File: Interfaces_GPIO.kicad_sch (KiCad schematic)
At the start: 5 parts, among them U3 MCP23008-xP

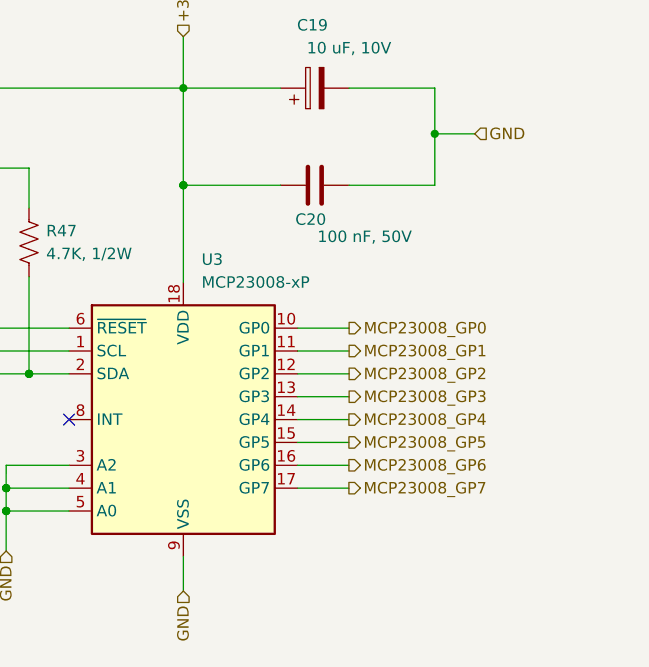
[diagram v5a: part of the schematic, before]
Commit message: Se finalizó con el PCB del prototipo.
Dado que se buscó a toda costa que el PCB fuera de 1 capa, en varios puntos del circuito se tuvieron que agregar pin headers individuales para conectar a 3V3 y GND, junto con tiras de pin headers. Cada una de estas se conectara luego entre si mediante cables.

Tambien se generaron los archivos Gerber y BOM.
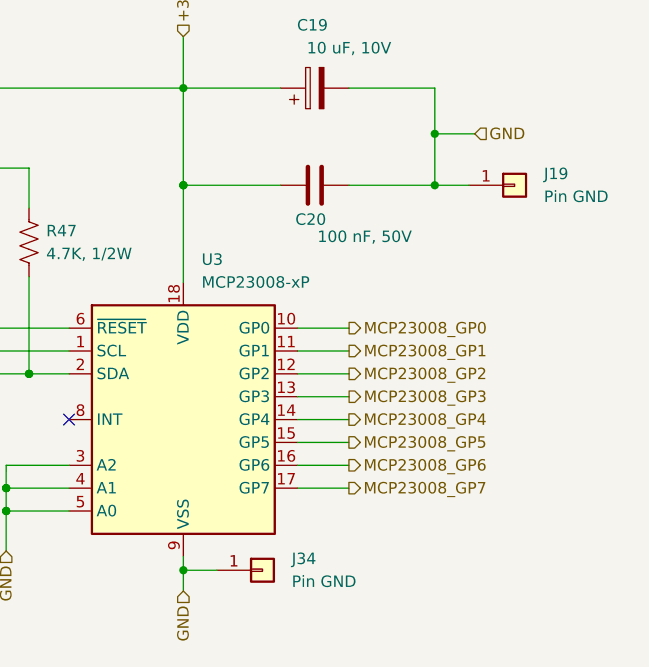
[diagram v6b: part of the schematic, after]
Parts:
- added J19, J34: Pin GND, Connector_PinHeader_2.54mm:PinHeader_1x01_P2.54mm_Vertical, symbol Connector_Generic:Conn_01x01
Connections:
- net GND: now also J19.1 (Pin_1), J34.1 (Pin_1)
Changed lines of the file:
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@@
 (kicad_sch (version 20211123) (generator eeschema)
   (paper "A4")
+  (junction (at 147.9804 131.0386) (diameter 0) (color 0 0 0 0)
+  )
   (junction (at 128.2954 124.46) (diameter 0) (color 0 0 0 0)
   )
@@
   )
   (junction (at 128.2903 124.46) (diameter 0) (color 0 0 0 0)
+  )
+  (junction (at 175.9153 88.265) (diameter 0) (color 0 0 0 0)
   )
   (junction (at 119.4003 106.68) (diameter 0) (color 0 0 0 0)
@@
     (stroke (width 0) (type default) (color 0 0 0 0))
   )
-  (wire (pts (xy 175.9153 88.265) (xy 166.3903 88.265))
+  (wire (pts (xy 166.3903 88.265) (xy 175.9153 88.265))
     (stroke (width 0) (type default) (color 0 0 0 0))
   )
@@
     (stroke (width 0) (type default) (color 0 0 0 0))
   )
+  (wire (pts (xy 175.9153 88.265) (xy 179.705 88.265))
+    (stroke (width 0) (type default) (color 0 0 0 0))
+  )
   (wire (pts (xy 128.2954 121.92) (xy 128.2903 121.92))
     (stroke (width 0) (type default) (color 0 0 0 0))
@@
     (stroke (width 0) (type default) (color 0 0 0 0))
   )
+  (wire (pts (xy 147.9804 131.0386) (xy 147.9804 133.35))
+    (stroke (width 0) (type default) (color 0 0 0 0))
+  )
   (wire (pts (xy 112.4153 106.68) (xy 119.4003 106.68))
     (stroke (width 0) (type default) (color 0 0 0 0))
@@
     (stroke (width 0) (type default) (color 0 0 0 0))
   )
-  (wire (pts (xy 147.9804 129.54) (xy 147.9804 133.35))
+  (wire (pts (xy 147.9804 129.54) (xy 147.9804 131.0386))
     (stroke (width 0) (type default) (color 0 0 0 0))
   )
@@
   )
   (wire (pts (xy 130.8303 86.36) (xy 130.8303 90.805))
+    (stroke (width 0) (type default) (color 0 0 0 0))
+  )
+  (wire (pts (xy 147.9804 131.0386) (xy 151.6888 131.0386))
     (stroke (width 0) (type default) (color 0 0 0 0))
   )
@@
   (hierarchical_label "+3,3V" (shape input) (at 147.9753 71.755 90)
     (effects (font (size 1.27 1.27)) (justify left))
+  )
+  (symbol (lib_id "Connector_Generic:Conn_01x01") (at 184.785 88.265 0) (unit 1)
+    (in_bom yes) (on_board yes) (fields_autoplaced)
+    (property "Reference" "J19" (id 0) (at 188.0362 86.9949 0)
+      (effects (font (size 1.27 1.27)) (justify left))
+    )
+    (property "Value" "Pin GND" (id 1) (at 188.0362 89.5349 0)
+      (effects (font (size 1.27 1.27)) (justify left))
+    )
+    (property "Footprint" "Connector_PinHeader_2.54mm:PinHeader_1x01_P2.54mm_Vertical" (id 2) (at 184.785 88.265 0)
+      (effects (font (size 1.27 1.27)) hide)
+    )
+    (property "Datasheet" "~" (id 3) (at 184.785 88.265 0)
+      (effects (font (size 1.27 1.27)) hide)
+    )
+    (pin "1")
   )
   (symbol (lib_id "Device:C") (at 162.5803 88.265 90) (unit 1)
@@
     (pin "9")
   )
+  (symbol (lib_id "Connector_Generic:Conn_01x01") (at 156.7688 131.0386 0) (unit 1)
+    (in_bom yes) (on_board yes) (fields_autoplaced)
+    (property "Reference" "J34" (id 0) (at 160.02 129.7685 0)
+      (effects (font (size 1.27 1.27)) (justify left))
+    )
+    (property "Value" "Pin GND" (id 1) (at 160.02 132.3085 0)
+      (effects (font (size 1.27 1.27)) (justify left))
+    )
+    (property "Footprint" "Connector_PinHeader_2.54mm:PinHeader_1x01_P2.54mm_Vertical" (id 2) (at 156.7688 131.0386 0)
+      (effects (font (size 1.27 1.27)) hide)
+    )
+    (property "Datasheet" "~" (id 3) (at 156.7688 131.0386 0)
+      (effects (font (size 1.27 1.27)) hide)
+    )
+    (pin "1")
+  )
 )

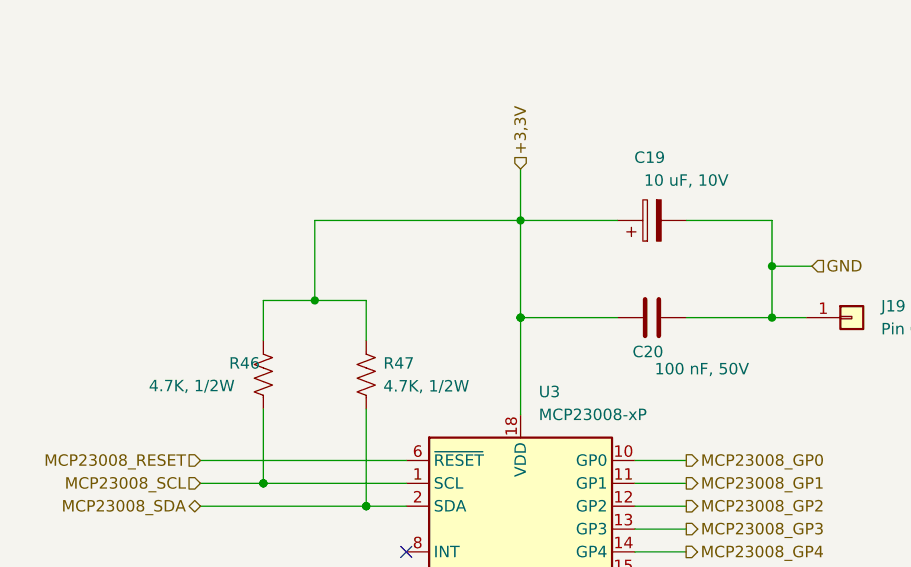
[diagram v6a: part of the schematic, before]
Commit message: Se modificaron algunos componentes, según disponibilidad
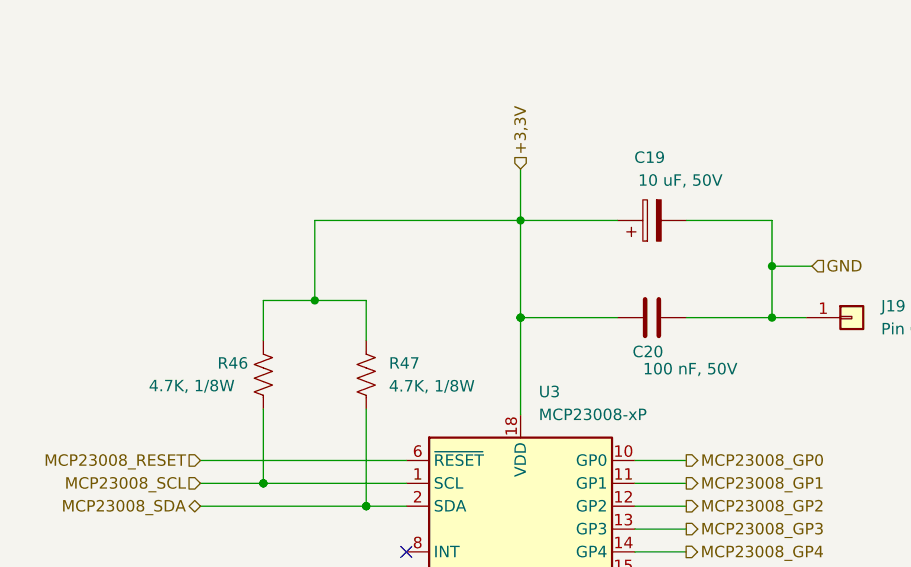
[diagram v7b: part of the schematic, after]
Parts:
- C19: value 10 uF, 10V -> 10 uF, 50V
- R46, R47: value 4.7K, 1/2W -> 4.7K, 1/8W
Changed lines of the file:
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@@
       (effects (font (size 1.27 1.27)) (justify left))
     )
-    (property "Value" "100 nF, 50V" (id 1) (at 173.3753 93.98 90)
+    (property "Value" "100 nF, 50V" (id 1) (at 172.085 93.98 90)
       (effects (font (size 1.27 1.27)) (justify left))
     )
@@
   (symbol (lib_id "Device:R_US") (at 130.8303 94.615 0) (unit 1)
     (in_bom yes) (on_board yes) (fields_autoplaced)
-    (property "Reference" "R47" (id 0) (at 132.7353 93.3449 0)
+    (property "Reference" "R47" (id 0) (at 133.35 93.3449 0)
       (effects (font (size 1.27 1.27)) (justify left))
     )
-    (property "Value" "4.7K, 1/2W" (id 1) (at 132.7353 95.8849 0)
+    (property "Value" "4.7K, 1/8W" (id 1) (at 133.35 95.8849 0)
       (effects (font (size 1.27 1.27)) (justify left))
     )
@@
     (in_bom yes) (on_board yes)
     (property "Reference" "C19" (id 0) (at 162.3263 70.485 90))
-    (property "Value" "10 uF, 10V" (id 1) (at 166.3903 73.025 90))
+    (property "Value" "10 uF, 50V" (id 1) (at 165.735 73.025 90))
     (property "Footprint" "Capacitor_SMD:C_0805_2012Metric" (id 2) (at 166.3903 76.5048 0)
       (effects (font (size 1.27 1.27)) hide)
@@
   (symbol (lib_id "Device:R_US") (at 119.4003 94.615 0) (unit 1)
     (in_bom yes) (on_board yes)
-    (property "Reference" "R46" (id 0) (at 115.5903 93.345 0)
+    (property "Reference" "R46" (id 0) (at 114.3 93.345 0)
       (effects (font (size 1.27 1.27)) (justify left))
     )
-    (property "Value" "4.7K, 1/2W" (id 1) (at 106.6749 95.8596 0)
+    (property "Value" "4.7K, 1/8W" (id 1) (at 106.6749 95.8596 0)
       (effects (font (size 1.27 1.27)) (justify left))
     )

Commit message: Finalización de rerouteo de PCB.
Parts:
- removed J19: Pin GND, Connector_PinHeader_2.54mm:PinHeader_1x01_P2.54mm_Vertical, symbol Connector_Generic:Conn_01x01
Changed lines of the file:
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@@
   (junction (at 128.2903 124.46) (diameter 0) (color 0 0 0 0)
-  )
-  (junction (at 175.9153 88.265) (diameter 0) (color 0 0 0 0)
   )
   (junction (at 119.4003 106.68) (diameter 0) (color 0 0 0 0)
@@
     (stroke (width 0) (type default) (color 0 0 0 0))
   )
-  (wire (pts (xy 175.9153 88.265) (xy 179.705 88.265))
-    (stroke (width 0) (type default) (color 0 0 0 0))
-  )
   (wire (pts (xy 128.2954 121.92) (xy 128.2903 121.92))
     (stroke (width 0) (type default) (color 0 0 0 0))
@@
     (effects (font (size 1.27 1.27)) (justify left))
   )
-  (symbol (lib_id "Connector_Generic:Conn_01x01") (at 184.785 88.265 0) (unit 1)
-    (in_bom yes) (on_board yes) (fields_autoplaced)
-    (property "Reference" "J19" (id 0) (at 188.0362 86.9949 0)
-      (effects (font (size 1.27 1.27)) (justify left))
-    )
-    (property "Value" "Pin GND" (id 1) (at 188.0362 89.5349 0)
-      (effects (font (size 1.27 1.27)) (justify left))
-    )
-    (property "Footprint" "Connector_PinHeader_2.54mm:PinHeader_1x01_P2.54mm_Vertical" (id 2) (at 184.785 88.265 0)
-      (effects (font (size 1.27 1.27)) hide)
-    )
-    (property "Datasheet" "~" (id 3) (at 184.785 88.265 0)
-      (effects (font (size 1.27 1.27)) hide)
-    )
-    (pin "1")
-  )
   (symbol (lib_id "Device:C") (at 162.5803 88.265 90) (unit 1)
